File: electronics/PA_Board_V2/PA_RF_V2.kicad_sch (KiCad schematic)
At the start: 80 parts, among them J1 Conn_Coaxial, J5 Conn_Coaxial, J7 Conn_Coaxial, J8 Conn_Coaxial, K1 G6E, Q2 BC848W, U1 PSA4-5043+, U14 Directional_Coupler, U3 PSA4-5043+, U4 RA35H1516M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

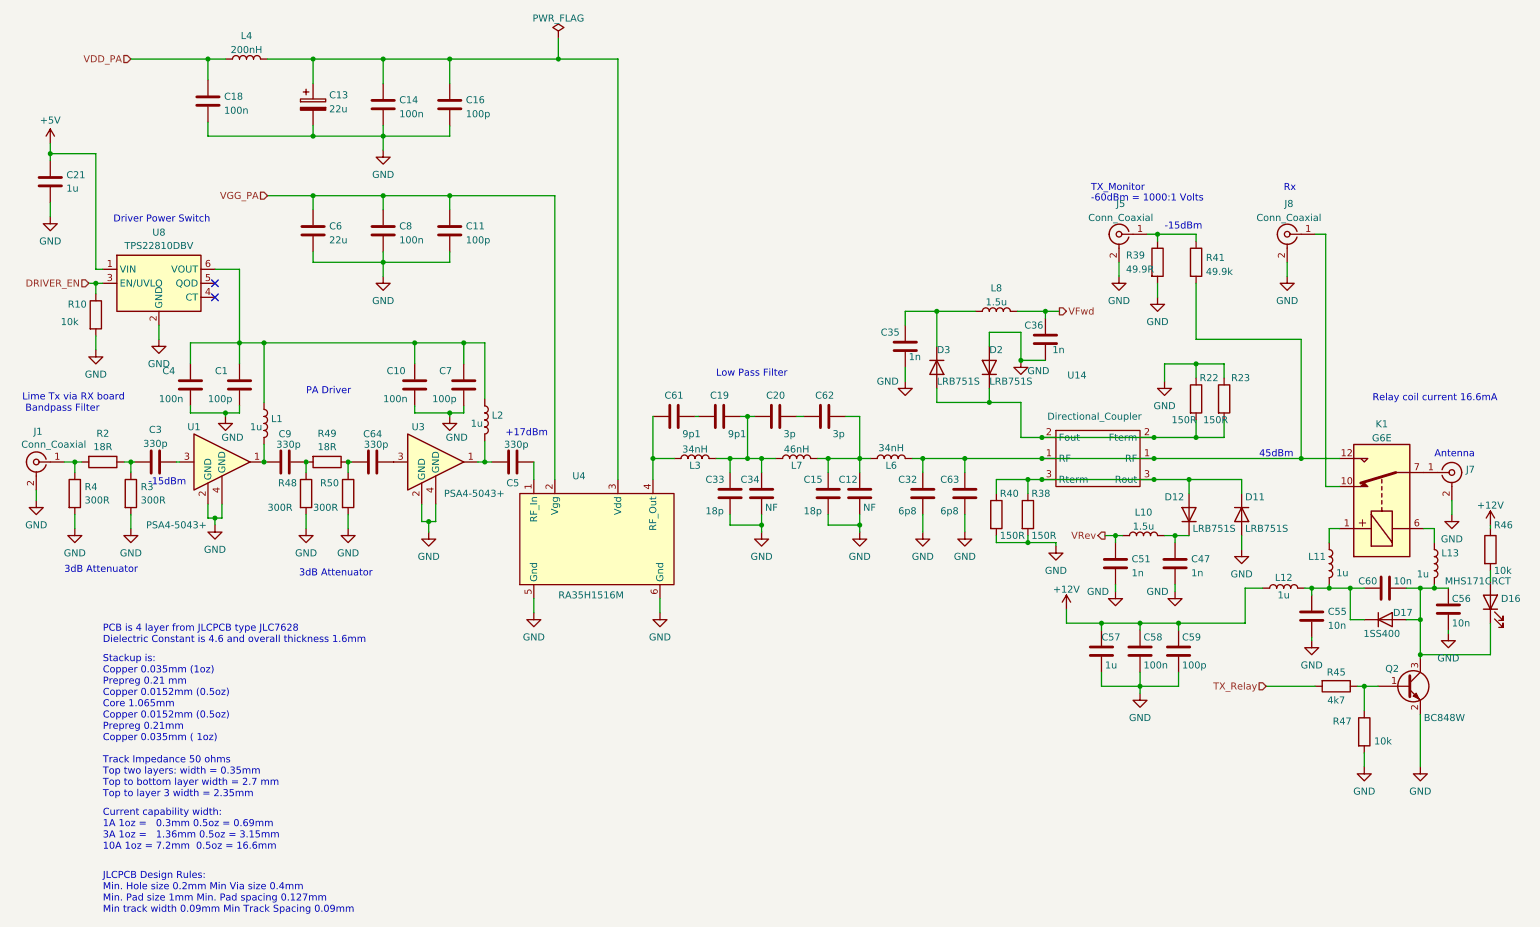
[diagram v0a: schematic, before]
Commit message: Update Arduino documentation and change to Kicad V8
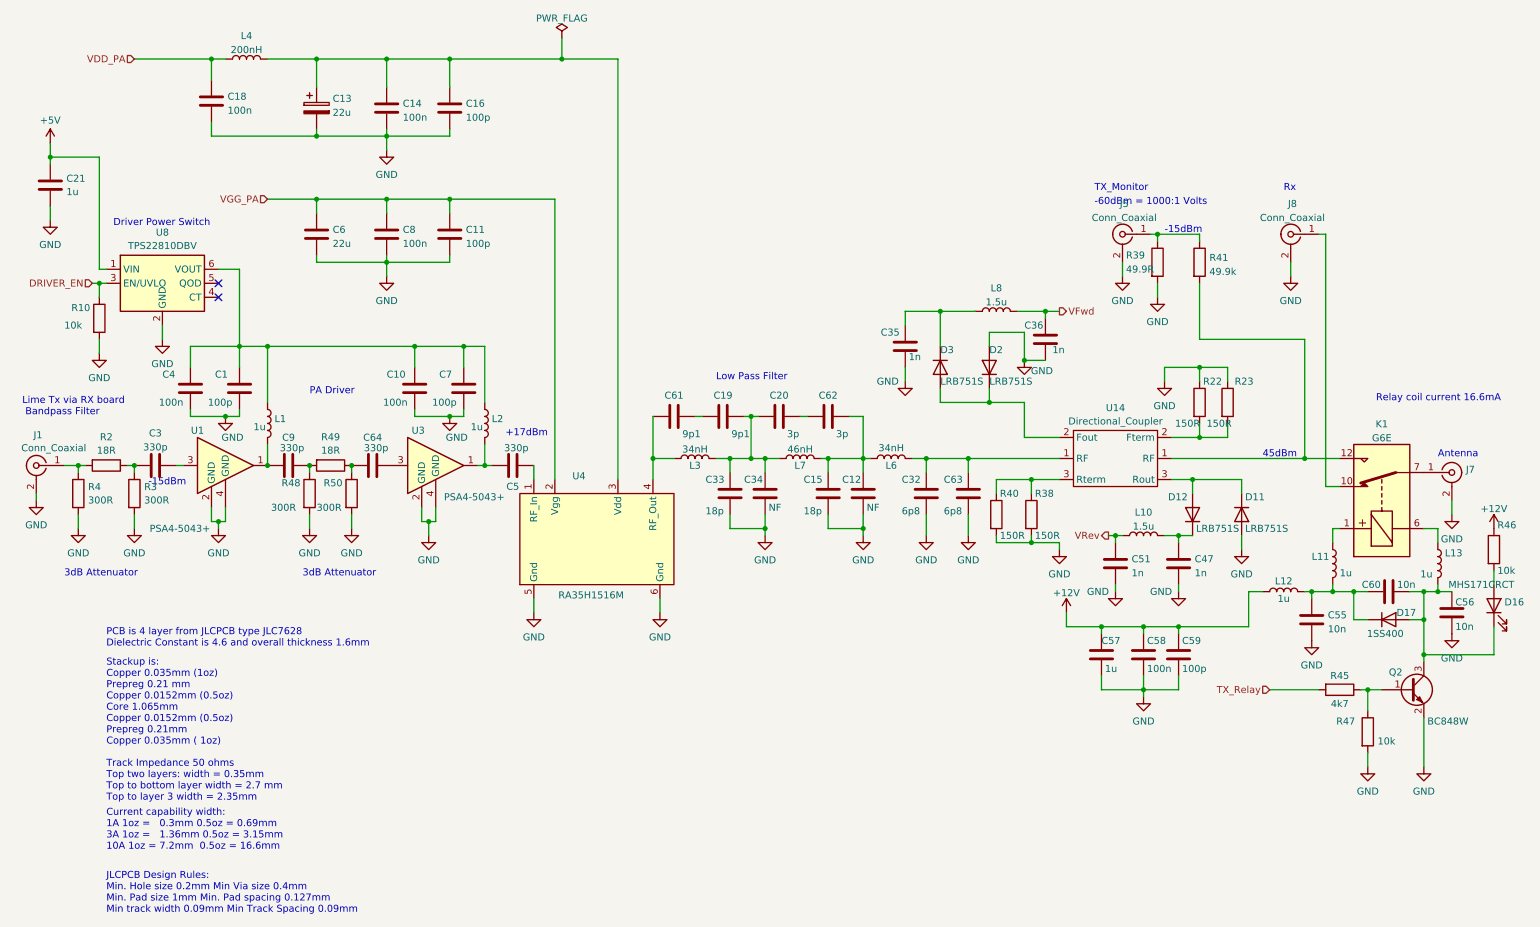
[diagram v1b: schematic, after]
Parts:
- U1, U3: footprint Pi_Tx_V2:MM1362 PSA4-5043+ -> Package_TO_SOT_SMD:SOT-343_SC-70-4
- U14: Comment not fitted -> (none)
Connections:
- net at C32.1, C63.1, L6.2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: no longer K1.12, R41.2
- net at D2.1 (K), D3.2 (A), U14.2 (Fterm): no longer R22.2, R23.2
- net at D11.1 (K), D12.2 (A), U14.3 (Rterm): no longer R38.1, R40.1
- new net: K1.12, R41.2, U14.1 (RF)
- new net: R22.2, R23.2, U14.2 (Fterm)
- new net: R38.1, R40.1, U14.3 (Rterm)
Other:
- moved on the sheet: C1, C10, C11, C12, C13, C14, C16, C18, C19, C20, C21, C3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
